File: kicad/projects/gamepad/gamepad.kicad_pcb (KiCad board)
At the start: 2 copper layers, 203.2 x 97.8 mm, 75 parts, among them J1 peripheral_addr_bus_connector, J10 Pad 2 SNES, J11 Conn_01x03_Pin, J2 peripheral_aux_connector, J3 peripheral_membank_connector, J4 PAD 1 ACTIVE, J5 PAD 2 ACTIVE, J6 Conn_02x05_Odd_Even, J7 Pad 1 header, J8 Pad 1 SNES, J9 Pad 2 header, U1 74HC161, U10 74HC245, U11 74HC245, U12 74HC245, U13 74HC245, U14 74HC00, U2 74HC161, U3 74HC595, U4 74HC595, U5 74HC595, U6 74HC595, U7 74HC14, U8 74HC00, U9 74HC161

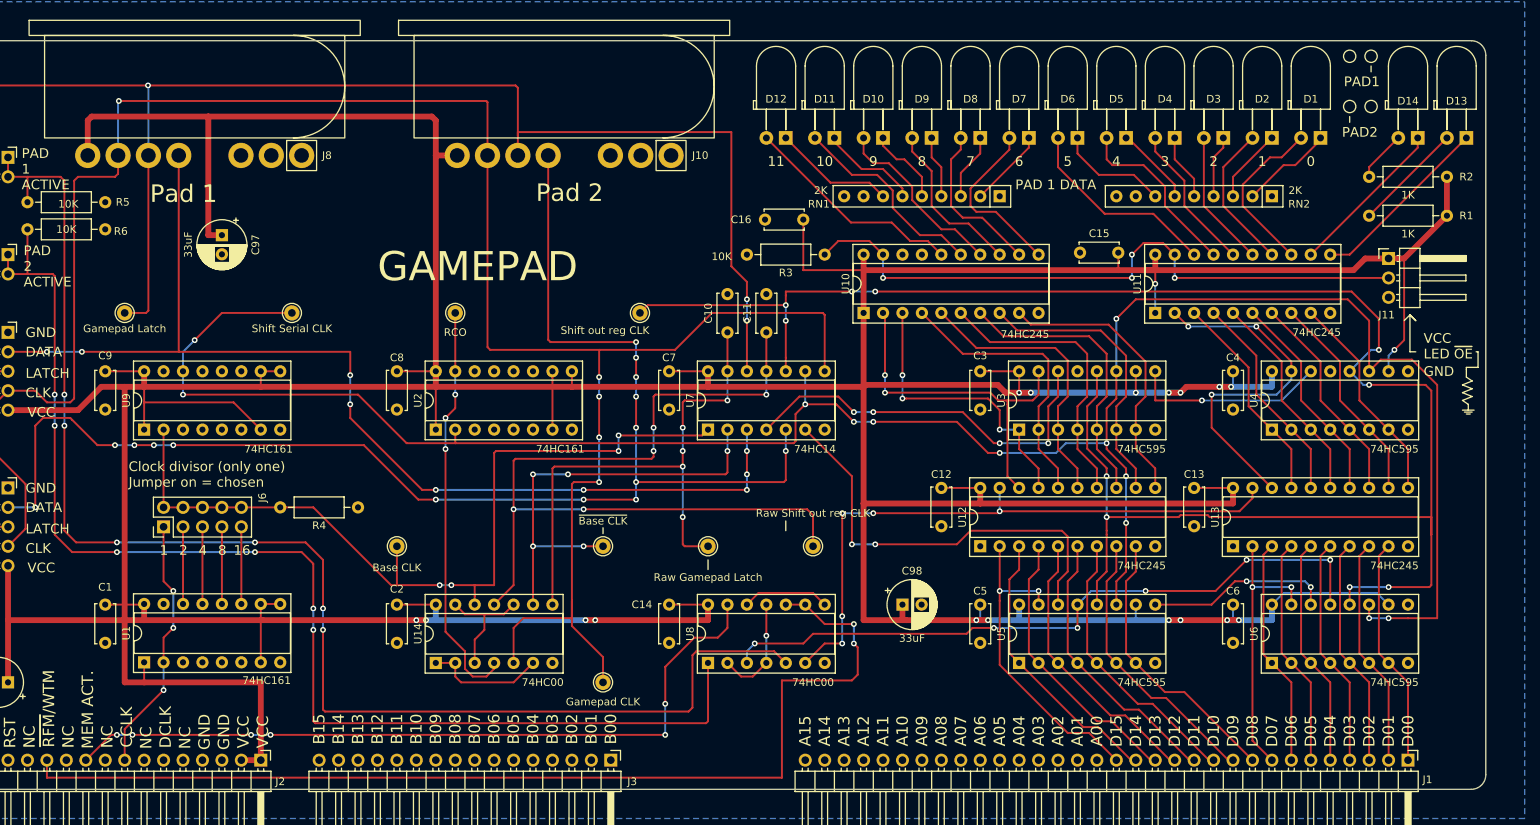
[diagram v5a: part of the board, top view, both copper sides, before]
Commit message: Gamepad updates. Fix memactive RFM. Fix miswired Pad 1 data and pas 1 and 2 read LEDs.
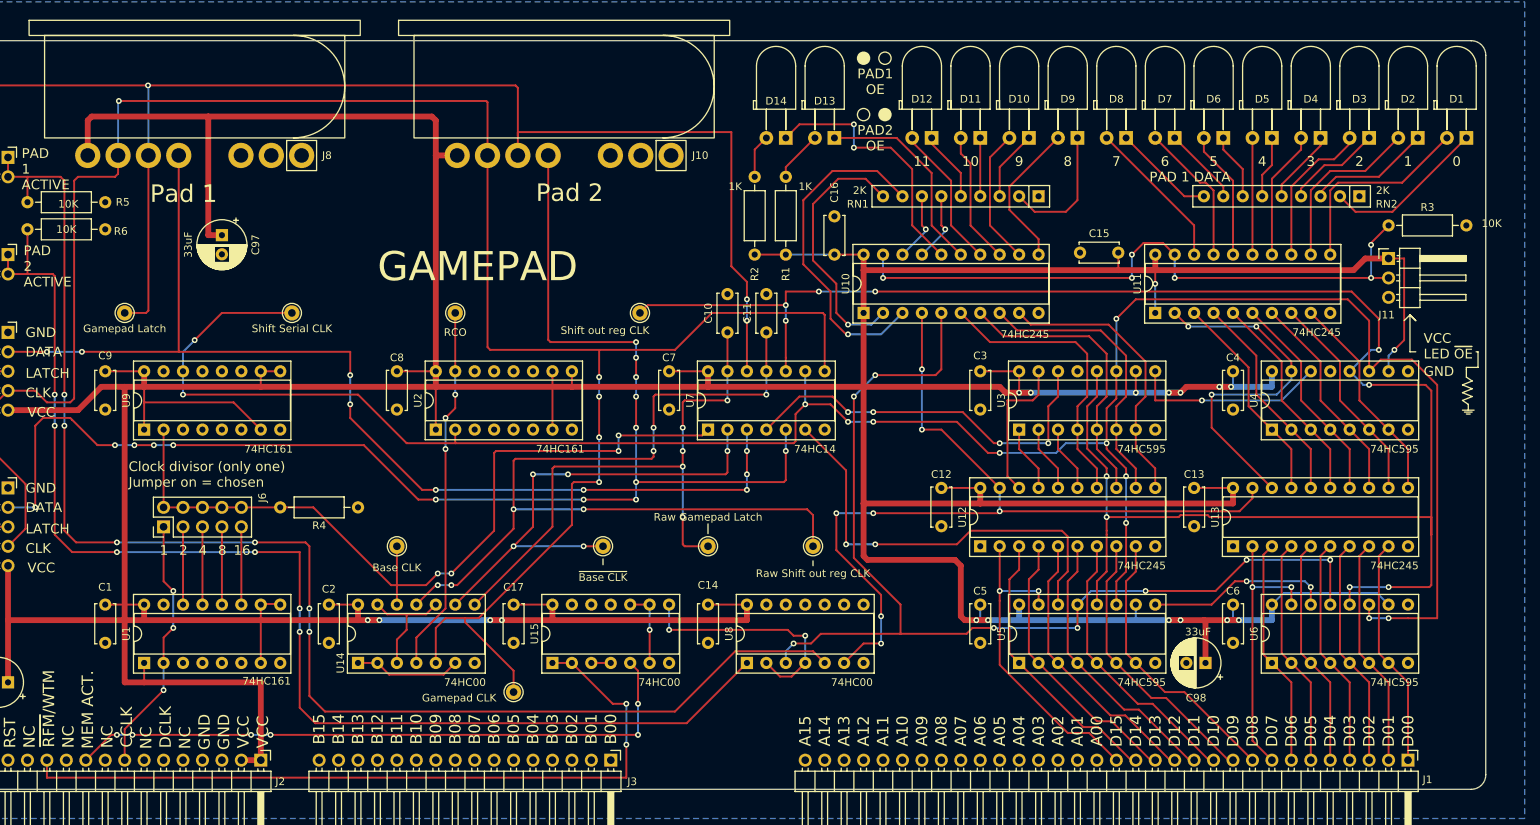
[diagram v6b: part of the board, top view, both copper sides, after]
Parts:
- added C17: C, Capacitor_THT:C_Disc_D5.0mm_W2.5mm_P5.00mm, F.Cu at (127.0, 124.5)
- added U15: 74HC00, Package_DIP:DIP-14_W7.62mm_Socket, F.Cu at (132.1, 132.1)
- moved D13 82.6 mm to (168.9, 63.5)
- moved D14 82.6 mm to (162.6, 63.5)
- moved R2 80.3 mm to (158.5, 68.6), turned to -90 degrees
- moved R1 76.4 mm to (162.6, 68.6), turned to -90 degrees
- moved R3 73.8 mm to (241.3, 74.9), turned to 0 degrees
- moved C98 40.3 mm to (217.4, 132.1), turned to 180 degrees
- moved D1 19.1 mm to (251.5, 63.5)
- moved D10 19.1 mm to (194.3, 63.5)
- moved D11 19.1 mm to (188.0, 63.5)
- moved D12 19.1 mm to (181.6, 63.5)
- moved D2 19.1 mm to (245.1, 63.5)
- moved D5 19.1 mm to (226.1, 63.5)
- moved D6 19.1 mm to (219.7, 63.5)
- moved D7 19.1 mm to (213.4, 63.5)
- moved D3 19.0 mm to (238.8, 63.5)
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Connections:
- D13 pad 1: /PAD 1 ADDR LED -> /PAD 2 ADDR LED
- D14 pad 1: /PAD 2 ADDR LED -> /PAD 1 ADDR LED
- RN1 pad 2: Net-(D7-K) -> Net-(D9-K)
- RN1 pad 3: Net-(D8-K) -> Net-(D10-K)
- RN1 pad 4: Net-(D9-K) -> Net-(D11-K)
- RN1 pad 5: Net-(D10-K) -> Net-(D12-K)
- RN1 pad 6: Net-(D11-K) -> Net-(RN1-R5)
- RN1 pad 7: Net-(D12-K) -> Net-(RN1-R6)
- RN1 pad 8: unconnected-(RN1-R7-Pad8) -> Net-(RN1-R7)
- RN1 pad 9: unconnected-(RN1-R8-Pad9) -> Net-(RN1-R8)
- RN2 pad 8: unconnected-(RN2-R7-Pad8) -> Net-(D7-K)
- RN2 pad 9: unconnected-(RN2-R8-Pad9) -> Net-(D8-K)
- U10 pad 11: /PAD 1 LED 6 -> /PAD 1 LED 8
- U10 pad 12: /PAD 1 LED 7 -> /PAD 1 LED 9
- U10 pad 13: /PAD 1 LED 8 -> /PAD 1 LED 10
- U10 pad 14: /PAD 1 LED 9 -> /PAD 1 LED 11
- U10 pad 15: /PAD 1 LED 10 -> /PAD 2 ADDR LED
- U10 pad 16: /PAD 1 LED 11 -> /PAD 1 ADDR LED
- U10 pad 17: unconnected-(U10-B2-Pad17) -> Net-(RN1-R5)
- U10 pad 18: unconnected-(U10-B1-Pad18) -> Net-(RN1-R6)
- U10 pad 2: /PAD 1 SHIFT 15 -> Net-(RN1-R8)
- U10 pad 3: /PAD 1 SHIFT 14 -> Net-(RN1-R7)
- U10 pad 4: /PAD 1 SHIFT 13 -> /PAD 1 ~{OE}
- U10 pad 5: /PAD 1 SHIFT 12 -> /PAD 2 ~{OE}
- U11 pad 11: /PAD 1 ADDR LED -> /PAD 1 LED 0
- U11 pad 12: /PAD 2 ADDR LED -> /PAD 1 LED 1
- U11 pad 13: /PAD 1 LED 0 -> /PAD 1 LED 2
- U11 pad 14: /PAD 1 LED 1 -> /PAD 1 LED 3
- U11 pad 15: /PAD 1 LED 2 -> /PAD 1 LED 4
- U11 pad 16: /PAD 1 LED 3 -> /PAD 1 LED 5
- U11 pad 17: /PAD 1 LED 4 -> /PAD 1 LED 6
- U11 pad 18: /PAD 1 LED 5 -> /PAD 1 LED 7
- U8 pad 10: /RFM_WTM -> GND
- U8 pad 11: /MEMACTIVE_RFM -> unconnected-(U8-Pad11)
- U8 pad 12: Net-(U8-Pad12) -> GND
- U8 pad 13: /MEM_ACTIVE -> GND
- U8 pad 8: Net-(U8-Pad12) -> unconnected-(U8-Pad8)
- U8 pad 9: /RFM_WTM -> GND
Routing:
- net /PAD 2 ~{OE}: track 90.3 -> 139.0 mm, vias 6 -> 8
- net Net-(RN1-R7): track 0.00 -> 44.3 mm, vias 0 -> 1
- net /RFM_WTM: track 138.0 -> 99.5 mm
- net Net-(RN1-R8): track 0.00 -> 34.3 mm, vias 0 -> 1
- net /PAD 1 ~{OE}: track 81.7 -> 113.4 mm, vias 5 -> 7
- net /PAD 1 SHIFT 14: track 38.3 -> 8.67 mm, vias 3 -> 0
- net /PAD 1 SHIFT 13: track 37.4 -> 8.67 mm
- net /PAD 1 SHIFT 12: track 37.3 -> 8.67 mm
- net /PAD 1 SHIFT 15: track 46.4 -> 19.5 mm, vias 2 -> 0
- net /MEMACTIVE_RFM: track 14.2 -> 31.5 mm, vias 1 -> 2
- net /MEM_ACTIVE: track 99.2 -> 83.3 mm
- net Net-(U8-Pad12): track 11.4 -> 0.00 mm
- net /PAD 1 LED 11: track 29.2 -> 18.9 mm
- net Net-(U15-Pad10): track 0.00 -> 10.2 mm, vias 0 -> 1
- net /PAD 1 ADDR LED: track 24.1 -> 34.2 mm, vias 0 -> 2
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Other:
- board text added: "PAD1 OE"
- board text added: "PAD2 OE"
- board text removed: "PAD1"
- board text removed: "PAD2"

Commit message: Part way through simplifying gamepad PCB.
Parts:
- removed C14: C, Capacitor_THT:C_Disc_D5.0mm_W2.5mm_P5.00mm
- removed TP2: Shift out reg CLK, Connector_Pin:Pin_D1.0mm_L10.0mm
- removed TP3: Shift Serial CLK, Connector_Pin:Pin_D1.0mm_L10.0mm
- removed TP7: RCO, Connector_Pin:Pin_D1.0mm_L10.0mm
- removed TP8: Raw Gamepad Latch, Connector_Pin:Pin_D1.0mm_L10.0mm
- removed TP9: Raw Shift out reg CLK, Connector_Pin:Pin_D1.0mm_L10.0mm
- removed U14: 74HC00, Package_DIP:DIP-14_W7.62mm_Socket
- added R10: 10K, Resistor_THT:R_Axial_DIN0207_L6.3mm_D2.5mm_P10.16mm_Horizontal, F.Cu at (98.6, 72.9)
- added R7: 10K, Resistor_THT:R_Axial_DIN0207_L6.3mm_D2.5mm_P10.16mm_Horizontal, F.Cu at (32.1, 32.6)
- added R8: 10K, Resistor_THT:R_Axial_DIN0207_L6.3mm_D2.5mm_P10.16mm_Horizontal, F.Cu at (32.1, 36.6)
- added R9: 4K7, Resistor_THT:R_Axial_DIN0207_L6.3mm_D2.5mm_P10.16mm_Horizontal, F.Cu at (103.1, 84.1)
- C10, C11: value C -> 30pF
- TP4: value Gamepad CLK -> TC
- U2: value 74HC161 -> 74HC123
- moved C11 62.1 mm to (98.6, 79.8), turned to 0 degrees
- moved TP4 55.8 mm to (141.7, 82.0), turned to -90 degrees
- moved C10 51.8 mm to (103.2, 88.6), turned to 0 degrees
- moved C2 44.4 mm to (147.3, 124.5)
- moved TP6 18.3 mm to (157.0, 115.8)
- moved C17 15.2 mm to (111.8, 124.5)
- moved U15 15.2 mm to (116.8, 132.1)
- moved R4 10.2 mm to (106.7, 121.9), turned to 90 degrees
- moved TP5 5.11 mm to (116.8, 116.3)
- moved U8 5.08 mm to (152.4, 132.1)
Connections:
- C10 pad 1: Net-(C10-Pad1) -> Net-(U2A-RCext)
- C10 pad 2: GND -> Net-(U2A-Cext)
- C11 pad 1: Net-(C11-Pad1) -> Net-(U2B-RCext)
- J10 pad 6: /GAMEPAD CLK -> /BASE CLK
- J7 pad 4: /GAMEPAD CLK -> /BASE CLK
- J8 pad 6: /GAMEPAD CLK -> /BASE CLK
- J9 pad 4: /GAMEPAD CLK -> /BASE CLK
- TP4 pad 1: /GAMEPAD CLK -> /TC
- U2 pad 1: VCC -> GND
- U2 pad 10: VCC -> GND
- U2 pad 11: unconnected-(U2-Q3-Pad11) -> VCC
- U2 pad 13: unconnected-(U2-Q1-Pad13) -> /GAMEPAD LATCH
- U2 pad 14: unconnected-(U2-Q0-Pad14) -> Net-(U2A-Cext)
- U2 pad 15: Net-(U2-TC) -> Net-(U2A-RCext)
- U2 pad 2: /SHIFT SERIAL CLK -> /TC
- U2 pad 3: GND -> VCC
- U2 pad 4: GND -> unconnected-(U2A-~{Q}-Pad4)
- U2 pad 5: GND -> unconnected-(U2B-Q-Pad5)
- U2 pad 7: VCC -> Net-(U2B-RCext)
- U2 pad 9: VCC -> GND
- U3 pad 11: /SHIFT SERIAL CLK -> /~{BASE CLK}
- U3 pad 12: /SHIFT OUT REG CLK -> /TC
- U4 pad 11: /SHIFT SERIAL CLK -> /~{BASE CLK}
- U4 pad 12: /SHIFT OUT REG CLK -> /TC
- U5 pad 11: /SHIFT SERIAL CLK -> /~{BASE CLK}
- U5 pad 12: /SHIFT OUT REG CLK -> /TC
- U6 pad 11: /SHIFT SERIAL CLK -> /~{BASE CLK}
- U6 pad 12: /SHIFT OUT REG CLK -> /TC
- U7 pad 10: /SHIFT OUT REG CLK -> unconnected-(U7-Pad10)
- U7 pad 11: Net-(C11-Pad1) -> GND
- U7 pad 12: /GAMEPAD LATCH -> unconnected-(U7-Pad12)
- U7 pad 13: Net-(C10-Pad1) -> GND
- U7 pad 8: /GAMEPAD CLK -> unconnected-(U7-Pad8)
- U7 pad 9: /SHIFT SERIAL CLK -> GND
- U9 pad 14: /SHIFT SERIAL CLK -> unconnected-(U9-Q0-Pad14)
- U9 pad 15: unconnected-(U9-TC-Pad15) -> /TC
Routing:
- net /TC: track 0.00 -> 311.6 mm, vias 0 -> 11
- net /SHIFT SERIAL CLK: track 291.9 -> 0.00 mm, vias 12 -> 0
- net /GAMEPAD CLK: track 278.5 -> 0.00 mm, vias 5 -> 0
- net /SHIFT OUT REG CLK: track 245.5 -> 0.00 mm, vias 10 -> 0
- net /BASE CLK: track 108.7 -> 253.4 mm
- net /~{BASE CLK}: track 64.0 -> 186.3 mm, vias 5 -> 9
- net Net-(C11-Pad1): track 118.5 -> 0.00 mm, vias 7 -> 0
- net Net-(C10-Pad1): track 75.9 -> 0.00 mm, vias 5 -> 0
- net Net-(U2-TC): track 47.8 -> 0.00 mm, vias 3 -> 0
- net VCC: track 889.4 -> 854.9 mm, vias 19 -> 15
- net /GAMEPAD LATCH: track 239.7 -> 209.2 mm, vias 3 -> 1
- net /MEMACTIVE_RFM: track 31.5 -> 12.7 mm, vias 2 -> 1
- net Net-(U14-Pad10): track 15.5 -> 0.00 mm
- net Net-(U14-Pad1): track 14.0 -> 0.00 mm
- net /RFM_WTM: track 99.5 -> 87.6 mm
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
